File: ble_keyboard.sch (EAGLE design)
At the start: 21 parts, among them CN1 FH34SRJ-6S, CN2 FH34SRJ-10S, CON2 41002W90-NP-S-30, Q1 DMG6968U-7, U1 YJ-14015

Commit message: Sikscreen cleanup before Gerberization
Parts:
- renumbered CIN_VIN to CON3
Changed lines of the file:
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@@
 </part>
 <part name="GND7" library="logic-supply" deviceset="GND" device=""/>
-<part name="CIN_VIN" library="con-molex" deviceset="53?-04" device="047"/>
+<part name="CON3" library="con-molex" deviceset="53?-04" device="047"/>
 <part name="+3V5" library="supply1" deviceset="+3V3" device=""/>
 <part name="GND8" library="logic-supply" deviceset="GND" device=""/>
@@
 </instance>
 <instance part="GND7" gate="1" x="22.86" y="139.7" rot="MR0"/>
-<instance part="CIN_VIN" gate="-1" x="17.78" y="154.94" rot="MR0"/>
-<instance part="CIN_VIN" gate="-2" x="17.78" y="152.4" smashed="yes" rot="MR0">
+<instance part="CON3" gate="-1" x="17.78" y="154.94" rot="MR0"/>
+<instance part="CON3" gate="-2" x="17.78" y="152.4" smashed="yes" rot="MR0">
 <attribute name="NAME" x="15.24" y="151.638" size="1.524" layer="95" rot="MR0"/>
 </instance>
-<instance part="CIN_VIN" gate="-3" x="17.78" y="149.86" rot="MR0"/>
-<instance part="CIN_VIN" gate="-4" x="17.78" y="147.32" rot="MR0"/>
+<instance part="CON3" gate="-3" x="17.78" y="149.86" rot="MR0"/>
+<instance part="CON3" gate="-4" x="17.78" y="147.32" rot="MR0"/>
 <instance part="+3V5" gate="G$1" x="78.74" y="162.56" smashed="yes" rot="MR0">
 <attribute name="VALUE" x="75.692" y="165.354" size="1.778" layer="96" rot="MR180"/>
@@
 </segment>
 <segment>
-<pinref part="CIN_VIN" gate="-4" pin="S"/>
+<pinref part="CON3" gate="-4" pin="S"/>
 <pinref part="GND7" gate="1" pin="GND"/>
 <wire x1="20.32" y1="147.32" x2="22.86" y2="147.32" width="0.1524" layer="91"/>
@@
 <wire x1="27.94" y1="134.62" x2="45.72" y2="134.62" width="0.1524" layer="91"/>
 <label x="45.72" y="134.62" size="1.27" layer="95" font="vector" xref="yes"/>
-<pinref part="CIN_VIN" gate="-2" pin="S"/>
+<pinref part="CON3" gate="-2" pin="S"/>
 <wire x1="27.94" y1="152.4" x2="20.32" y2="152.4" width="0.1524" layer="91"/>
 </segment>
@@
 <wire x1="25.4" y1="132.08" x2="45.72" y2="132.08" width="0.1524" layer="91"/>
 <label x="45.72" y="132.08" size="1.27" layer="95" font="vector" xref="yes"/>
-<pinref part="CIN_VIN" gate="-3" pin="S"/>
+<pinref part="CON3" gate="-3" pin="S"/>
 <wire x1="25.4" y1="149.86" x2="20.32" y2="149.86" width="0.1524" layer="91"/>
 </segment>
@@
 <net name="LIPO_RAW" class="0">
 <segment>
-<pinref part="CIN_VIN" gate="-1" pin="S"/>
+<pinref part="CON3" gate="-1" pin="S"/>
 <pinref part="VREG1" gate="VREG" pin="VIN"/>
 <wire x1="55.88" y1="154.94" x2="50.8" y2="154.94" width="0.1524" layer="91"/>

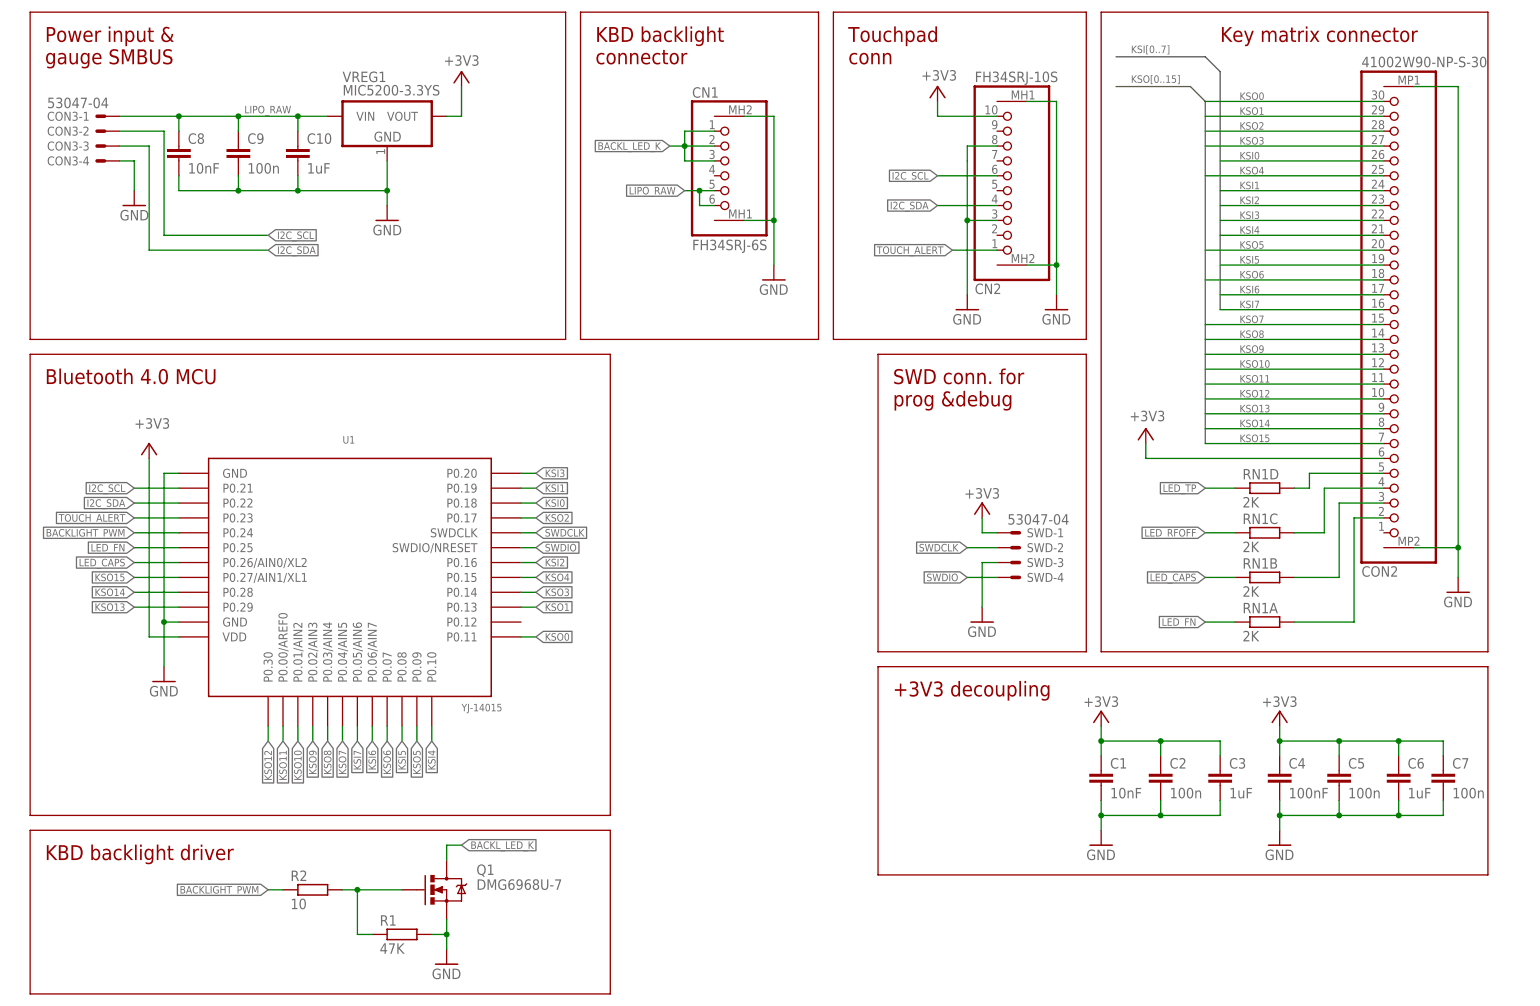
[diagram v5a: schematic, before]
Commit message: Updated BT module footprint
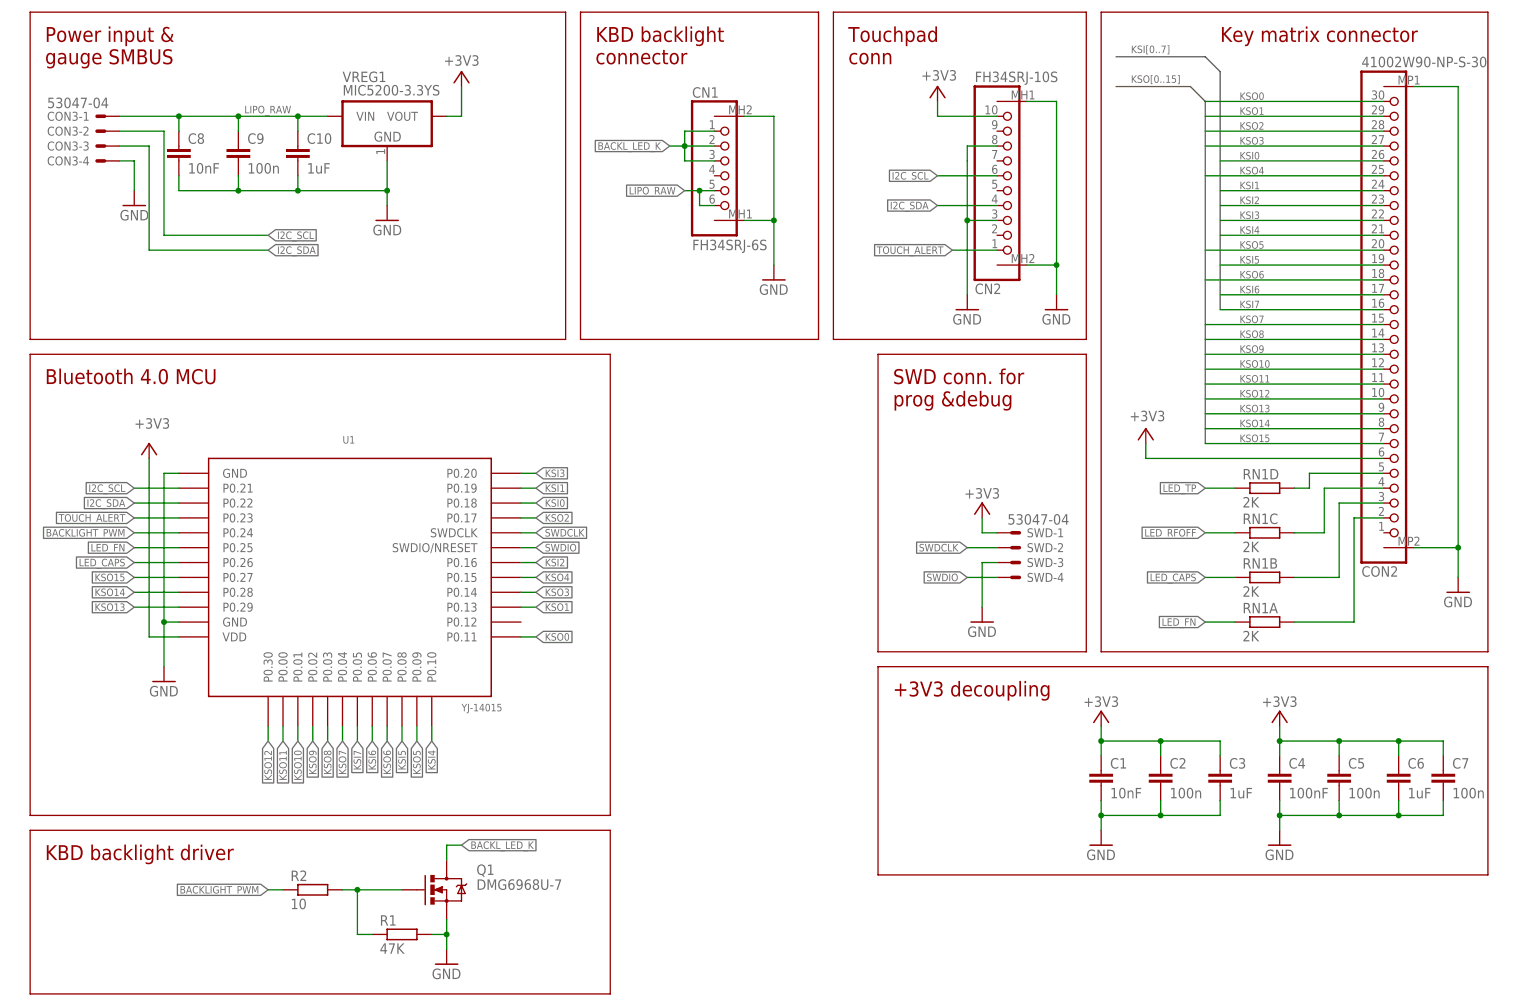
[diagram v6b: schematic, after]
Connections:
- net KSI6: now also U1.P0.06; no longer U1.P0.06/AIN7
- net KSI7: now also U1.P0.05; no longer U1.P0.05/AIN6
- net KSO10: now also U1.P0.01; no longer U1.P0.01/AIN2
- net KSO11: now also U1.P0.00; no longer U1.P0.00/AREF0
- net KSO15: now also U1.P0.27; no longer U1.P0.27/AIN1/XL1
- net KSO7: now also U1.P0.04; no longer U1.P0.04/AIN5
- net KSO8: now also U1.P0.03; no longer U1.P0.03/AIN4
- net KSO9: now also U1.P0.02; no longer U1.P0.02/AIN3
- net LED_CAPS: now also U1.P0.26; no longer U1.P0.26/AIN0/XL2
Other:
- moved on the sheet: CN1, CN2, CON2

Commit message: Schematic cleanup
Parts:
- removed CN1: FH34SRJ-6S, hirose_FH34SRJ:FH34SRJ-6S
- removed CN2: FH34SRJ-10S, hirose_FH34SRJ:FH34SRJ-10S
- removed CON2: 41002W90-NP-S-30, JTC41002:41002W90-NP-S-30
- removed CON3: 53047-04, con-molex:53047-04
- added BACKLIGHT: FH34SRJ-6S, hirose_FH34SRJ:FH34SRJ-6S
- added KEYBOARD: 41002W90-NP-S-30, JTC41002:41002W90-NP-S-30
- added PWR: 53047-04, con-molex:53047-04
- added Q2: DMG2305UX-7, transistor-fet:BSA223SP
- added R3: 47K, rcl:R-EU_R0603
- added TOUCHPAD: FH34SRJ-10S, hirose_FH34SRJ:FH34SRJ-10S
- RN1: value 2K -> 1K5; OC_TME (none) -> DR1206-1K5-4/8
- VREG1: value MIC5200-3.3YS -> MCP1703T-3302E/DB; OC_TME MIC5200-3.3YS -> MCP1703T-3302E/DB
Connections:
- removed net N$1: CON2.5, RN1D.2
- removed net N$2: CON2.4, RN1C.2
- removed net N$3: CON2.3, RN1B.2
- removed net N$4: CON2.2, RN1A.2
- new net LED_CAPS_R: KEYBOARD.3, RN1B.2
- new net LED_FN_R: KEYBOARD.2, RN1A.2
- new net LED_RFOFF_R: KEYBOARD.4, RN1C.2
- new net LED_TP_R: KEYBOARD.5, RN1D.2
- new net NENABLE_TOUCHPAD: Q2.G, R3.1, U1.P0.12
- new net V_TOUCHPAD: Q2.D, TOUCHPAD.10
- net +3V3: now also KEYBOARD.6, Q2.S, R3.2; no longer CN2.10, CON2.6
- net BACKL_LED_K: now also BACKLIGHT.1, BACKLIGHT.2, BACKLIGHT.3; no longer CN1.1, CN1.2, CN1.3
- net GND: now also BACKLIGHT.MH1, BACKLIGHT.MH2, KEYBOARD.MP1, KEYBOARD.MP2, PWR-4.S, TOUCHPAD.3, TOUCHPAD.8, TOUCHPAD.MH1, TOUCHPAD.MH2; no longer CN1.MH1, CN1.MH2, CN2.3, CN2.8, CN2.MH1, CN2.MH2, CON2.MP1, CON2.MP2, CON3-4.S
- net I2C_SCL: now also PWR-2.S, TOUCHPAD.6; no longer CN2.6, CON3-2.S
- net I2C_SDA: now also PWR-3.S, TOUCHPAD.4; no longer CN2.4, CON3-3.S
- net KSI0: now also KEYBOARD.26; no longer CON2.26
- net KSI1: now also KEYBOARD.24; no longer CON2.24
- net KSI2: now also KEYBOARD.23; no longer CON2.23
- net KSI3: now also KEYBOARD.22; no longer CON2.22
- net KSI4: now also KEYBOARD.21; no longer CON2.21
- net KSI5: now also KEYBOARD.19; no longer CON2.19
- net KSI6: now also KEYBOARD.17; no longer CON2.17
- net KSI7: now also KEYBOARD.16; no longer CON2.16
- net KSO0: now also KEYBOARD.30; no longer CON2.30
- net KSO1: now also KEYBOARD.29; no longer CON2.29
- net KSO10: now also KEYBOARD.12; no longer CON2.12
- net KSO11: now also KEYBOARD.11; no longer CON2.11
- net KSO12: now also KEYBOARD.10; no longer CON2.10
- net KSO13: now also KEYBOARD.9; no longer CON2.9
- net KSO14: now also KEYBOARD.8; no longer CON2.8
- net KSO15: now also KEYBOARD.7; no longer CON2.7
- net KSO2: now also KEYBOARD.28; no longer CON2.28
- net KSO3: now also KEYBOARD.27; no longer CON2.27
- net KSO4: now also KEYBOARD.25; no longer CON2.25
- net KSO5: now also KEYBOARD.20; no longer CON2.20
- net KSO6: now also KEYBOARD.18; no longer CON2.18
- net KSO7: now also KEYBOARD.15; no longer CON2.15
- net KSO8: now also KEYBOARD.14; no longer CON2.14
- net KSO9: now also KEYBOARD.13; no longer CON2.13
- net LIPO_RAW: now also BACKLIGHT.5, BACKLIGHT.6, PWR-1.S; no longer CN1.5, CN1.6, CON3-1.S
- net TOUCH_ALERT: now also TOUCHPAD.1; no longer CN2.1
